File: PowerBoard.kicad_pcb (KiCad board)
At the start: 2 copper layers, 131 x 131 mm, 94 parts, among them IC1 LTC7004HMSE#PBF, IC2 LTC7004HMSE#PBF, IC3 LTC7004HMSE#PBF, J1 XT90, J10 DEAN_T, J11 DEAN_T, J12 DEAN_T, J13 DEAN_T, J14 DEAN_T, J15 DEAN_T, J16 XT60, J17 XT60, J18 XT60, J19 XT60, J2 DEAN_T, J20 XT60, J21 XT60, J22 XT30, J23 XT30, J24 XT30, J25 XT30, J26 XT30, J27 XT30, J28 XT90, J29 XT30, J3 XT60, J30 XT30, J31 XT30, J32 Conn_01x02, J4 XT30, J5 XT90, J6 XT90, J7 XT90, J8 XT90, J9 XT90, Q1 IRFS7437TRLPBF, Q2 IRFS7437TRLPBF, Q3 IRFS7437TRLPBF, U1 Pico, U2 LM317_TO-220

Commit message: iterate the layoutL
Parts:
- added C8: 1u, Capacitor_SMD:C_1206_3216Metric, F.Cu at (86.0, 45.0)
- added D13: LED, Diode_SMD:D_1206_3216Metric, F.Cu at (97.6, 73.5)
- added D14: LED, Diode_SMD:D_1206_3216Metric, F.Cu at (101.4, 84.5)
- added D17: LED, Diode_SMD:D_1206_3216Metric, F.Cu at (52.1, 38.5)
- added F4: Fuse, Fuse:Fuse_Blade_ATO_directSolder, F.Cu at (90.5, 78.5)
- added IC4: LT1910ES8#PBF, SamacSys_Parts:SOIC127P599X175-8N, F.Cu at (92.0, 46.5)
- added Q4: IRFS7437TRLPBF, Package_TO_SOT_SMD:TO-263-2, F.Cu at (92.0, 62.0)
- added R5: 6k8, Resistor_SMD:R_1206_3216Metric, F.Cu at (103.0, 73.5)
- added R6: 6k8, Resistor_SMD:R_1206_3216Metric, F.Cu at (106.5, 84.5)
- added R7: 3m, Resistor_SMD:R_Shunt_Isabellenhuette_BVR4026, F.Cu at (101.2, 49.5)
- added R8: 3m, Resistor_SMD:R_Shunt_Isabellenhuette_BVR4026, F.Cu at (34.7, 37.8)
- C5: value 0.1u -> 1u
- D6: value SMAJ58CA -> SMAJ48A
- D7: value LED -> SMAJ48A; footprint Diode_SMD:D_1206_3216Metric -> Diode_SMD:D_SMA
- IC1: value LTC7004HMSE#PBF -> LT1910ES8#PBF; footprint SamacSys_Parts:SOP50P490X110-11N -> SamacSys_Parts:SOIC127P599X175-8N
- moved R10 91.5 mm to (53.0, 30.8), turned to 0 degrees
- moved D7 87.7 mm to (50.4, 15.8)
- moved D10 87.2 mm to (52.1, 35.1), turned to 0 degrees
- moved R9 74.0 mm to (53.0, 27.5), turned to 0 degrees
- moved F1 69.2 mm to (169.2, 78.5)
- moved D6 49.3 mm to (56.7, 115.4)
- moved Q1 43.7 mm to (39.3, 19.7), turned to 0 degrees
- moved D8 40.3 mm to (57.1, 93.5), turned to 180 degrees
- moved C5 39.4 mm to (49.1, 19.7), turned to 0 degrees
- moved D9 36.2 mm to (67.5, 70.9)
- moved R2 32.8 mm to (72.0, 80.5)
- moved R1 25.4 mm to (64.0, 84.5), turned to 0 degrees
- moved Q2 18.5 mm to (27.8, 89.9)
- moved J2 13.4 mm to (114.5, 45.8), turned to 180 degrees
- moved F2 9.15 mm to (113.8, 78.5), turned to 0 degrees
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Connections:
- C5 pad 1: Net-(IC1-BST) -> Net-(IC1-GND)
- C5 pad 2: Net-(IC1-TS) -> GND
- D10 pad 2: 24V_2 -> Net-(D10-A)
- D6 pad 1: GND -> Net-(D6-A1)
- D6 pad 2: 42V_2 -> GND
- D7 pad 1: Net-(D7-K) -> Net-(D7-A1)
- D7 pad 2: Net-(D7-A) -> GND
- F2 pad 1: Net-(D7-A) -> Net-(D10-A)
- IC1 pad 1: +12V -> Net-(IC1-GND)
- IC1 pad 2: GND -> Net-(IC1-GND)
- IC1 pad 3: GND -> unconnected-(IC1-~{FAULT}-Pad3)
- IC1 pad 5: GND -> Net-(D7-A1)
- IC1 pad 6: Net-(IC1-TGDN) -> Net-(IC1-SENSE)
- IC1 pad 7: Net-(IC1-TGDN) -> unconnected-(IC1-NC-Pad7)
- IC1 pad 8: Net-(IC1-TS) -> Net-(D7-A1)
- Q1 pad 1: Net-(IC1-TGDN) -> Net-(D7-A1)
- Q1 pad 2: Net-(D7-A) -> Net-(D10-A)
- Q1 pad 3: +24V -> Net-(Q1-S)
- R10 pad 1: Net-(D10-K) -> Net-(D17-K)
- R9 pad 1: Net-(D7-K) -> Net-(D10-K)
- U1 pad 9: EN_48V -> EN_42V
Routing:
- net 5V_2: track 279.0 -> 101.4 mm, vias 4 -> 2
- net 42V_2: track 0.00 -> 174.0 mm, vias 0 -> 2
- net EN_42V: track 0.00 -> 129.6 mm, vias 0 -> 1
- net EN_48V: track 123.5 -> 0.00 mm
- net GND: track 954.6 -> 887.1 mm, vias 1 -> 21
- net Net-(D6-A1): track 0.00 -> 24.0 mm
- net Net-(D13-A): track 0.00 -> 22.2 mm
- net Net-(D7-A): track 16.4 -> 0.00 mm
- net Net-(D8-A): track 16.1 -> 0.00 mm
- net Net-(D11-A): track 14.0 -> 0.00 mm
- net +42V: track 84.0 -> 72.6 mm
- net Net-(IC4-SENSE): track 0.00 -> 8.35 mm
- net Net-(Q4-S): track 0.00 -> 6.88 mm
- net 24V_2: track 167.5 -> 162.2 mm
- net Net-(IC4-GND): track 0.00 -> 4.82 mm
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
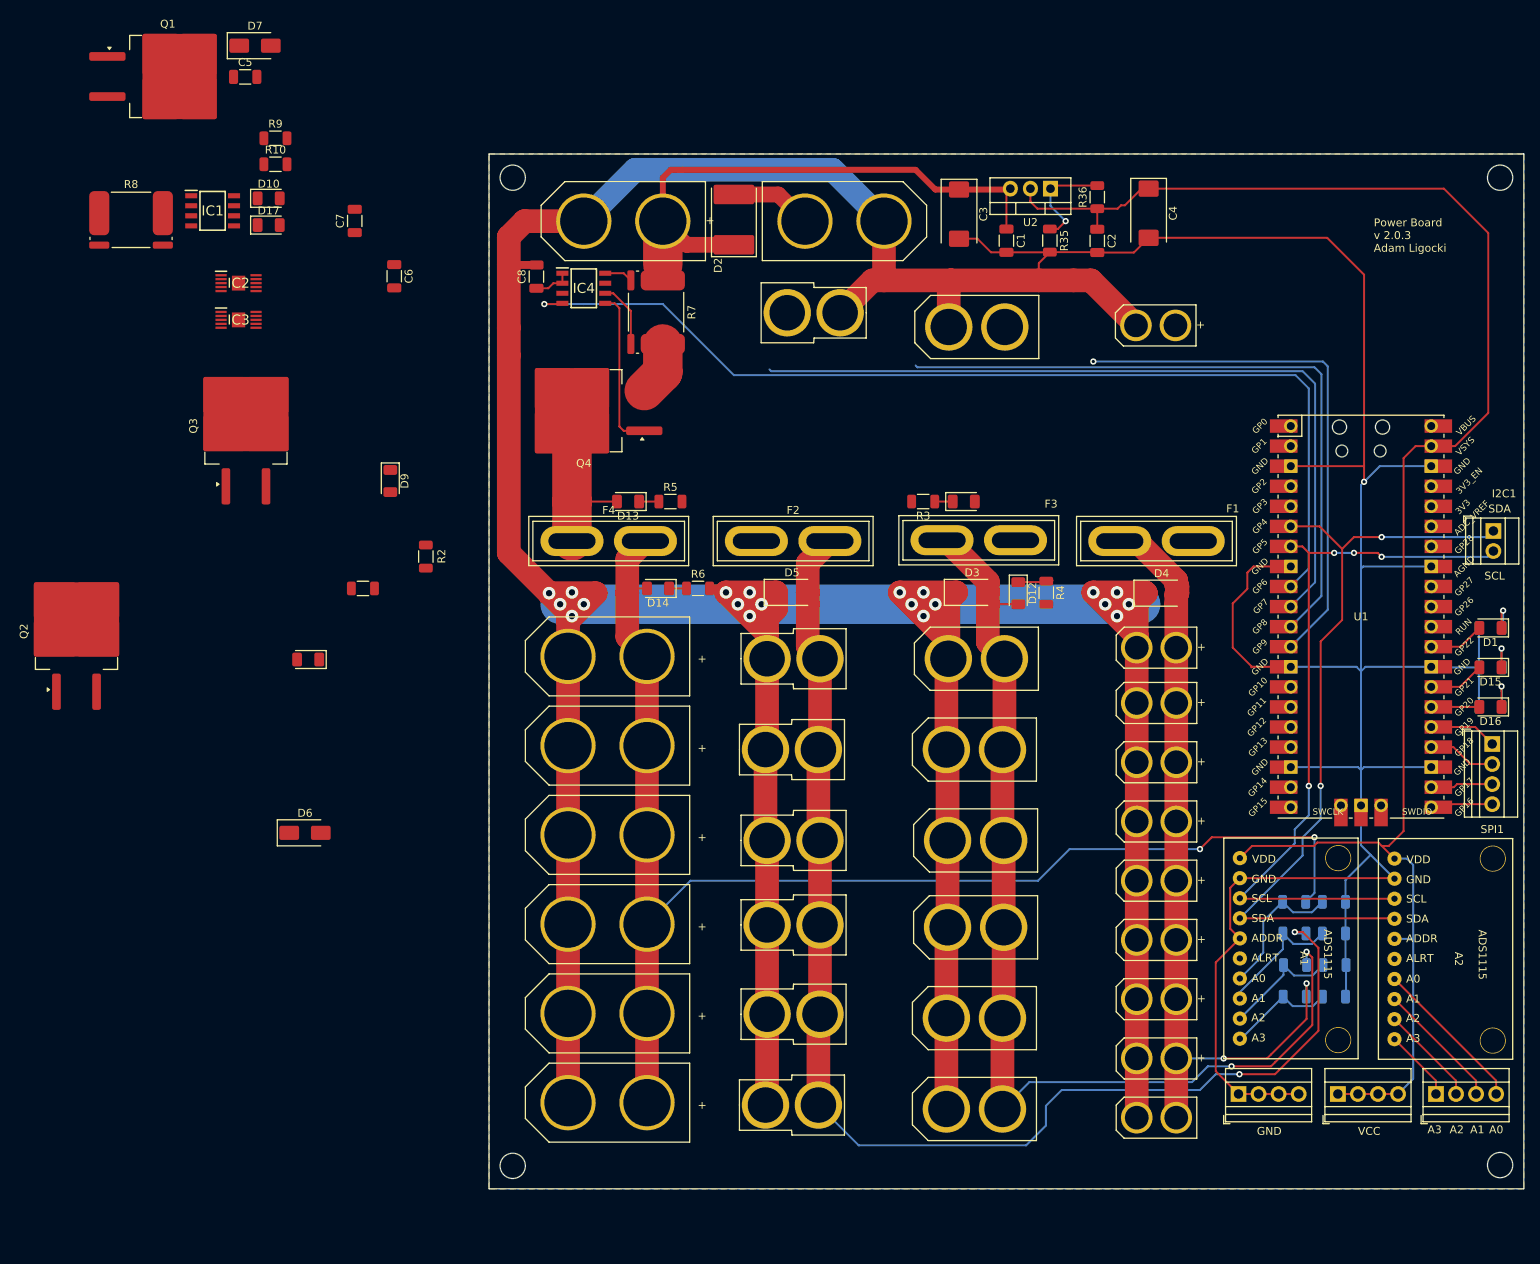
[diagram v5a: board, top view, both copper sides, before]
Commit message: fix the layout
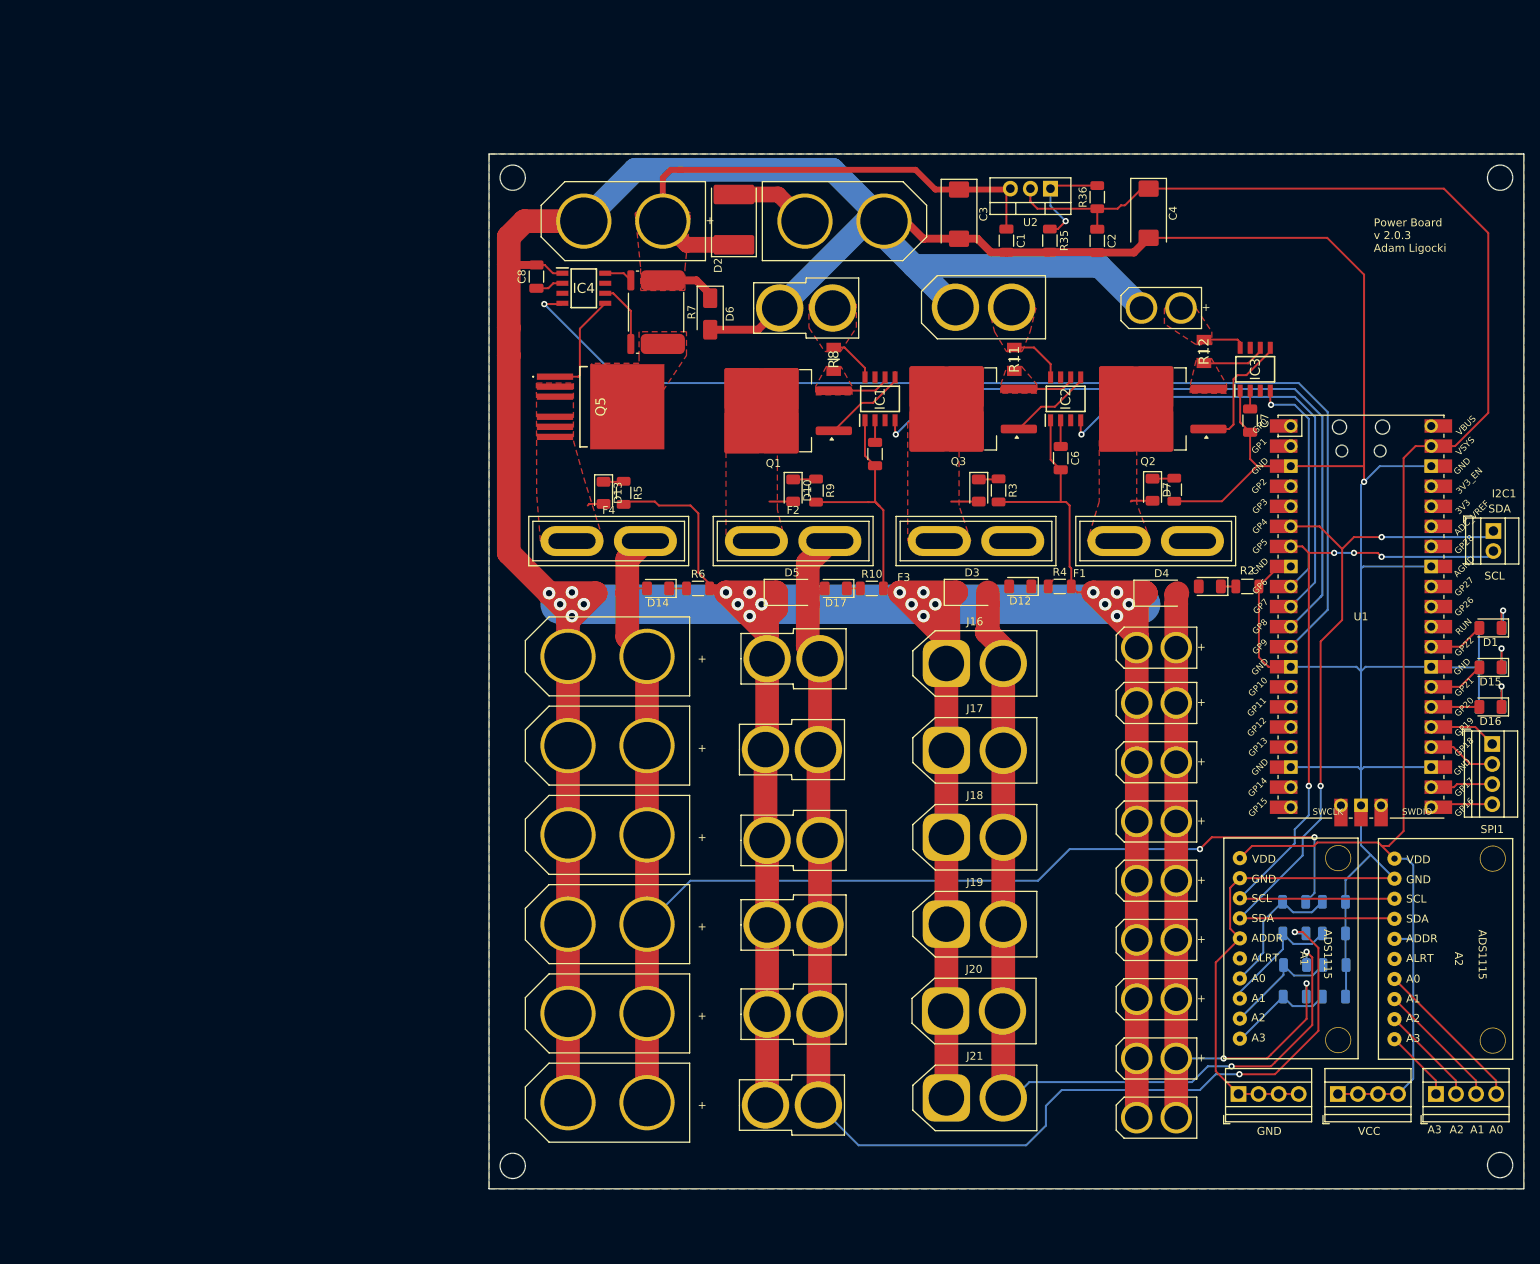
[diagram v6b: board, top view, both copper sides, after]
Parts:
- removed D9: LED, Diode_SMD:D_1206_3216Metric
- removed Q4: IRFS7437TRLPBF, Package_TO_SOT_SMD:TO-263-2
- added Q5: IRFS7530-7PPBF, SamacSys_Parts:IRFS41157PPBF, F.Cu at (94.1, 61.5)
- added R11: 5m, SamacSys_Parts:RESC3216X89N, F.Cu at (146.5, 55.5)
- added R12: 5m, SamacSys_Parts:RESC3216X89N, F.Cu at (170.5, 54.5)
- C6, C7: value 0.1u -> 1u
- D7: value SMAJ48A -> LED; footprint Diode_SMD:D_SMA -> Diode_SMD:D_1206_3216Metric
- IC2, IC3: value LTC7004HMSE#PBF -> LT1910ES8#PBF; footprint SamacSys_Parts:SOP50P490X110-11N -> SamacSys_Parts:SOIC127P599X175-8N
- J16, J17, J18, J19, J20, J21: footprint my_footprint_lib:XT60 -> Connector_AMASS:AMASS_XT60-F_1x02_P7.20mm_Vertical
- R7: value 3m -> 4m
- R8: value 3m -> 1m; footprint Resistor_SMD:R_Shunt_Isabellenhuette_BVR4026 -> SamacSys_Parts:RESC3216X89N
- moved Q2 138.5 mm to (163.4, 61.8), turned to 180 degrees
- moved IC3 128.9 mm to (177.0, 56.8), turned to 90 degrees
- moved D7 126.8 mm to (164.0, 72.0), turned to -90 degrees
- moved C7 116.1 mm to (176.3, 63.3), turned to -90 degrees
- moved D8 114.5 mm to (171.2, 84.2)
- moved IC2 105.7 mm to (153.0, 60.5), turned to 90 degrees
- moved R2 104.1 mm to (176.0, 84.2), turned to 0 degrees
- moved R1 103.5 mm to (166.8, 72.0), turned to -90 degrees
- moved C5 92.9 mm to (128.9, 67.5), turned to -90 degrees
- moved R10 92.7 mm to (128.5, 84.5)
- moved R8 90.7 mm to (123.6, 55.5), turned to 90 degrees
- moved Q3 90.2 mm to (139.4, 61.8), turned to 180 degrees
- moved IC1 87.8 mm to (129.5, 60.5), turned to 90 degrees
- moved Q1 87.6 mm to (116.0, 62.0), turned to 180 degrees
- moved C6 87.5 mm to (152.4, 68.0)
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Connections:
- C5 pad 1: Net-(IC1-GND) -> Net-(IC1-TIMER)
- C6 pad 1: Net-(IC2-BST) -> Net-(IC2-TIMER)
- C6 pad 2: Net-(IC2-TS) -> GND
- C7 pad 1: Net-(IC3-BST) -> Net-(IC3-TIMER)
- C7 pad 2: Net-(IC3-TS) -> GND
- C8 pad 1: Net-(IC4-GND) -> Net-(IC4-TIMER)
- D6 pad 1: Net-(D6-A1) -> +42V
- D7 pad 1: Net-(D7-A1) -> Net-(D7-K)
- D7 pad 2: GND -> Net-(D7-A)
- D8 pad 2: Net-(D8-A) -> 5V_2
- F1 pad 1: Net-(D8-A) -> Net-(D7-A)
- IC1 pad 1: Net-(IC1-GND) -> GND
- IC1 pad 2: Net-(IC1-GND) -> Net-(IC1-TIMER)
- IC1 pad 5: Net-(D7-A1) -> Net-(IC1-GATE)
- IC1 pad 8: Net-(D7-A1) -> +24V
- IC2 pad 1: +12V -> GND
- IC2 pad 2: GND -> Net-(IC2-TIMER)
- IC2 pad 3: GND -> unconnected-(IC2-~{FAULT}-Pad3)
- IC2 pad 4: EN_5V -> EN_12V
- IC2 pad 5: GND -> Net-(IC2-GATE)
- IC2 pad 6: Net-(IC2-TGDN) -> Net-(IC2-SENSE)
- IC2 pad 7: Net-(IC2-TGDN) -> unconnected-(IC2-NC-Pad7)
- IC2 pad 8: Net-(IC2-TS) -> +12V
- IC3 pad 1: +12V -> GND
- IC3 pad 2: GND -> Net-(IC3-TIMER)
- IC3 pad 3: GND -> unconnected-(IC3-~{FAULT}-Pad3)
- IC3 pad 4: EN_12V -> EN_5V
- IC3 pad 5: GND -> Net-(IC3-GATE)
- IC3 pad 6: Net-(IC3-TGDN) -> Net-(IC3-SENSE)
- IC3 pad 7: Net-(IC3-TGDN) -> unconnected-(IC3-NC-Pad7)
- IC3 pad 8: Net-(IC3-TS) -> +5V
- IC4 pad 1: Net-(IC4-GND) -> GND
- IC4 pad 2: Net-(IC4-GND) -> Net-(IC4-TIMER)
- IC4 pad 5: Net-(D6-A1) -> Net-(IC4-GATE)
- IC4 pad 8: Net-(D6-A1) -> Net-(IC4-V+)
- J16 pad 1: 12V_2 -> GND
- J16 pad 2: GND -> 12V_2
- J17 pad 1: 12V_2 -> GND
- J17 pad 2: GND -> 12V_2
- J18 pad 1: 12V_2 -> GND
- J18 pad 2: GND -> 12V_2
- J19 pad 1: 12V_2 -> GND
- J19 pad 2: GND -> 12V_2
- J20 pad 1: 12V_2 -> GND
- J20 pad 2: GND -> 12V_2
- J21 pad 1: 12V_2 -> GND
- J21 pad 2: GND -> 12V_2
- Q1 pad 1: Net-(D7-A1) -> Net-(IC1-GATE)
- Q1 pad 3: Net-(Q1-S) -> Net-(IC1-SENSE)
- Q2 pad 1: Net-(IC2-TGDN) -> Net-(IC3-GATE)
- Q2 pad 2: Net-(D8-A) -> Net-(D7-A)
- Q2 pad 3: +5V -> Net-(IC3-SENSE)
- Q3 pad 1: Net-(IC3-TGDN) -> Net-(IC2-GATE)
- Q3 pad 3: +12V -> Net-(IC2-SENSE)
- R1 pad 1: Net-(D8-K) -> Net-(D7-K)
- R2 pad 1: Net-(D9-K) -> Net-(D8-K)
- R7 pad 1: Net-(Q4-S) -> +42V
- R7 pad 2: Net-(IC4-SENSE) -> Net-(IC4-V+)
- R7 pad 3: Net-(D6-A1) -> Net-(IC4-SENSE)
- R7 pad 4: +42V -> Net-(Q5-D)
- R8 pad 1: Net-(Q1-S) -> Net-(IC1-SENSE)
- R8 pad 2: Net-(IC1-SENSE) -> +24V
- U1 pad 10: EN_24V -> EN_12V
- U1 pad 11: EN_12V -> EN_24V
- U1 pad 12: EN_5V -> EN_42V
- U1 pad 9: EN_42V -> EN_5V
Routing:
- net GND: track 887.1 -> 1017.3 mm
- net EN_5V: track 67.4 -> 29.5 mm
- net EN_12V: track 85.4 -> 59.7 mm, vias 0 -> 1
- net Net-(D6-A1): track 24.0 -> 0.00 mm
- net Net-(D13-A): track 22.2 -> 2.08 mm
- net Net-(IC3-GATE): track 0.00 -> 15.7 mm
- net 12V_2: track 134.6 -> 119.8 mm
- net Net-(IC4-GATE): track 0.00 -> 13.7 mm
- net Net-(IC1-GATE): track 0.00 -> 11.5 mm
- net EN_24V: track 99.3 -> 88.0 mm, vias 0 -> 1
- net Net-(IC2-GATE): track 0.00 -> 10.8 mm
- net 5V_2: track 101.4 -> 91.5 mm
- net EN_42V: track 129.6 -> 138.8 mm
- net Net-(IC3-SENSE): track 0.00 -> 8.20 mm
- net Net-(IC1-SENSE): track 0.00 -> 7.43 mm
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- added copper zone on F.Cu, net +12V
- added copper zone on F.Cu, net +24V
- added copper zone on F.Cu, net +42V
- added copper zone on F.Cu, net +5V
- added copper zone on F.Cu, net Net-(D10-A)
- added copper zone on F.Cu, net Net-(D11-A)
- added copper zone on F.Cu, net Net-(D13-A)
- added copper zone on F.Cu, net Net-(D7-A)
- added copper zone on F.Cu, net Net-(IC1-SENSE)
- added copper zone on F.Cu, net Net-(IC2-SENSE)
- added copper zone on F.Cu, net Net-(IC3-SENSE)
- added copper zone on F.Cu, net Net-(Q5-D)

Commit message: Finish the design
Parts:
- removed A1, A2: ADS1115_ADC_Module, my_footprint_lib:ADS1115
- removed ADC1, SPI1: Screw_Terminal_01x04, TerminalBlock:TerminalBlock_Xinya_XY308-2.54-4P_1x04_P2.54mm_Horizontal
- removed C6: 1u, Capacitor_SMD:C_1206_3216Metric
- removed R25, R32: 100k, Resistor_SMD:R_1206_3216Metric
- removed R30: 33k, Resistor_SMD:R_1206_3216Metric
- removed R31, R33, R39, R40: 10k, Resistor_SMD:R_1206_3216Metric
- removed R35: 680R, Resistor_SMD:R_1206_3216Metric
- removed R36: 220R, Resistor_SMD:R_1206_3216Metric
- added C10: 22pF, Capacitor_SMD:C_1206_3216Metric, F.Cu at (147.0, 33.5)
- added C11: 3300pF, Capacitor_SMD:C_1206_3216Metric, F.Cu at (149.5, 33.5)
- added C12: 10u, Capacitor_SMD:C_1206_3216Metric, F.Cu at (141.0, 24.5)
- added C13: 1u, Capacitor_SMD:C_1206_3216Metric, F.Cu at (130.0, 26.0)
- added C9: 5.5nF, Capacitor_SMD:C_1206_3216Metric, F.Cu at (144.5, 33.5)
- added D18: LED, Diode_SMD:D_1206_3216Metric, F.Cu at (168.5, 76.5)
- added D19: LED, Diode_SMD:D_1206_3216Metric, F.Cu at (168.5, 82.0)
- added D9: SMAJ30CA, Diode_SMD:D_SMA, F.Cu at (68.0, 74.0)
- added F5: Fuse, Fuse:Fuse_Blade_ATO_directSolder, F.Cu at (54.4, 67.0)
- added G***: LOGO, LOGO, F.Cu at (152.5, 153.5)
- added H5: MountingHole, MountingHole:MountingHole_3.2mm_M3, F.Cu at (100.2, 93.0)
- added IC5: LT1910ES8#PBF, SamacSys_Parts:SOIC127P599X175-8N, F.Cu at (67.5, 60.0)
- added IC7: MAX17541GATB+T, SamacSys_Parts:SON50P200X300X80-11N, F.Cu at (141.6, 29.1)
- added J33: XT30, Connector_AMASS:AMASS_XT30U-F_1x02_P5.0mm_Vertical, F.Cu at (117.5, 88.5)
- added J34: XT30, Connector_AMASS:AMASS_XT30U-F_1x02_P5.0mm_Vertical, F.Cu at (117.5, 95.5)
- added J35: XT30, Connector_AMASS:AMASS_XT30U-F_1x02_P5.0mm_Vertical, F.Cu at (117.5, 102.5)
- added J36: XT30, Connector_AMASS:AMASS_XT30U-F_1x02_P5.0mm_Vertical, F.Cu at (117.5, 109.5)
- added J37: XT30, Connector_AMASS:AMASS_XT30U-F_1x02_P5.0mm_Vertical, F.Cu at (117.5, 116.5)
- added J38: XT30, Connector_AMASS:AMASS_XT30U-F_1x02_P5.0mm_Vertical, F.Cu at (117.5, 123.5)
- added J39: XT30, Connector_AMASS:AMASS_XT30U-F_1x02_P5.0mm_Vertical, F.Cu at (117.5, 130.5)
- added J40: XT30, Connector_AMASS:AMASS_XT30U-F_1x02_P5.0mm_Vertical, F.Cu at (117.5, 137.5)
- added J41: XT60, Connector_AMASS:AMASS_XT60-F_1x02_P7.20mm_Vertical, F.Cu at (76.5, 37.5)
- added L1: 470M, SamacSys_Parts:SRR5828A2R6Y, F.Cu at (147.5, 23.6)
- added Q4: IRFS7437TRLPBF, Package_TO_SOT_SMD:TO-263-2, F.Cu at (97.5, 51.0)
- added R13: 6k8, Resistor_SMD:R_1206_3216Metric, F.Cu at (98.5, 73.5)
- added R14: 5m, SamacSys_Parts:RESC3216X89N, F.Cu at (104.0, 44.5)
- added R15: 6k8, Resistor_SMD:R_1206_3216Metric, F.Cu at (57.0, 73.0)
- added R16: 80k, Resistor_SMD:R_1206_3216Metric, F.Cu at (140.0, 33.5)
- added R17: 17.5k, Resistor_SMD:R_1206_3216Metric, F.Cu at (135.5, 33.0)
- added R18: 10k, Resistor_SMD:R_1206_3216Metric, F.Cu at (170.0, 47.0)
- added R19: 10k, Resistor_SMD:R_1206_3216Metric, F.Cu at (167.0, 47.0)
- added R20: 10k, Resistor_SMD:R_1206_3216Metric, B.Cu at (141.5, 99.0)
- added R21: 21.5k, Resistor_SMD:R_1206_3216Metric, F.Cu at (148.0, 30.0)
- added R22: 10k, Resistor_SMD:R_1206_3216Metric, F.Cu at (171.5, 71.0)
- added R23: 10k, Resistor_SMD:R_1206_3216Metric, F.Cu at (171.5, 76.5)
- added R24: 10k, Resistor_SMD:R_1206_3216Metric, F.Cu at (171.5, 82.0)
- added U3: INA238, Package_SO:VSSOP-10_3x3mm_P0.5mm, F.Cu at (96.0, 27.0)
- added U4: INA238, Package_SO:VSSOP-10_3x3mm_P0.5mm, F.Cu at (105.0, 27.0)
- added U5: INA238, Package_SO:VSSOP-10_3x3mm_P0.5mm, F.Cu at (114.0, 27.0)
- added U6: INA238, Package_SO:VSSOP-10_3x3mm_P0.5mm, F.Cu at (123.0, 27.0)
- C3, C4: value 10u -> 1u; footprint Capacitor_Tantalum_SMD:CP_EIA-7343-15_Kemet-W -> Capacitor_SMD:C_1206_3216Metric
- D1: value LED -> SMAJ48A; footprint Diode_SMD:D_1206_3216Metric -> Diode_SMD:D_SMA
- D10: value LED -> SMAJ30CA; footprint Diode_SMD:D_1206_3216Metric -> Diode_SMD:D_SMA
- D11: value LED -> SMAJ15CA; footprint Diode_SMD:D_1206_3216Metric -> Diode_SMD:D_SMA
- D14: value LED -> SMAJ6.5CA; footprint Diode_SMD:D_1206_3216Metric -> Diode_SMD:D_SMA
- D3: value SMAJ15CA -> LED; footprint Diode_SMD:D_SMA -> Diode_SMD:D_1206_3216Metric
- D4: value SMAJ6.5CA -> LED; footprint Diode_SMD:D_SMA -> Diode_SMD:D_1206_3216Metric
- D5: value SMAJ30CA -> LED; footprint Diode_SMD:D_SMA -> Diode_SMD:D_1206_3216Metric
- D6: value SMAJ48A -> LED; footprint Diode_SMD:D_SMA -> Diode_SMD:D_1206_3216Metric
- J1, J6, J7, J8, J9: footprint my_footprint_lib:XT90 -> SamacSys_Parts:XT90
- J10, J11, J12, J13: value DEAN_T -> XT90; footprint my_footprint_lib:DEAN_T -> SamacSys_Parts:XT90
- J14, J15, J2: footprint my_footprint_lib:DEAN_T -> SamacSys_Parts:DEANS-T
- J16, J17, J18, J19: value XT60 -> DEAN_T; footprint Connector_AMASS:AMASS_XT60-F_1x02_P7.20mm_Vertical -> SamacSys_Parts:DEANS-T
- J22, J23, J24, J25, J26, J27, J29, J30, J31: value XT30 -> XT60; footprint my_footprint_lib:XT30 -> Connector_AMASS:AMASS_XT60-F_1x02_P7.20mm_Vertical
- J28: value XT90 -> XT60; footprint my_footprint_lib:XT90 -> Connector_AMASS:AMASS_XT60-F_1x02_P7.20mm_Vertical
- J3: footprint my_footprint_lib:XT60 -> Connector_AMASS:AMASS_XT60-F_1x02_P7.20mm_Vertical
- J32: value Conn_01x02 -> XT30; footprint my_footprint_lib:XT90 -> Connector_AMASS:AMASS_XT30U-F_1x02_P5.0mm_Vertical
- J5: value XT90 -> Conn_01x02; footprint my_footprint_lib:XT90 -> SamacSys_Parts:XT90
- Q1: value IRFS7437TRLPBF -> IRFS7530TRL7PP; footprint Package_TO_SOT_SMD:TO-263-2 -> SamacSys_Parts:IRFS7530TRL7PP
- Q5: value IRFS7530-7PPBF -> IRFS7437TRLPBF; footprint SamacSys_Parts:IRFS41157PPBF -> Package_TO_SOT_SMD:TO-263-2
- R1: value 6k8 -> 4m; footprint Resistor_SMD:R_1206_3216Metric -> Resistor_SMD:R_Shunt_Isabellenhuette_BVR4026
- R11: value 5m -> 1m
- R12: value 5m -> 6k8; footprint SamacSys_Parts:RESC3216X89N -> Resistor_SMD:R_1206_3216Metric
- R27, R29: value 100k -> 10k
- R7: value 4m -> 5m; footprint Resistor_SMD:R_Shunt_Isabellenhuette_BVR4026 -> SamacSys_Parts:RESC3216X89N
- R8: value 1m -> 5m
- U2: value LM317_TO-220 -> INA238; footprint Package_TO_SOT_THT:TO-220-3_Vertical -> Package_SO:VSSOP-10_3x3mm_P0.5mm
- moved D1 162.0 mm to (53.0, 38.5), turned to -90 degrees
- moved D16 149.6 mm to (59.5, 73.0), turned to 90 degrees
- moved IC3 141.7 mm to (37.0, 35.0), turned to 0 degrees
- moved D8 132.2 mm to (39.5, 73.0), turned to 90 degrees
- moved R1 124.5 mm to (47.0, 38.0)
- moved R4 114.8 mm to (40.0, 60.0), turned to -90 degrees
- moved R12 110.6 mm to (60.0, 60.0)
- moved C3 108.5 mm to (31.0, 34.0), turned to 90 degrees
- moved D15 107.8 mm to (101.0, 73.5), turned to 90 degrees
- moved F3 103.8 mm to (33.9, 67.0)
- moved R2 97.6 mm to (81.5, 60.0), turned to -90 degrees
- moved J15 91.4 mm to (58.0, 91.5)
- moved J14 90.9 mm to (58.0, 81.0)
- moved J25 87.2 mm to (73.9, 133.5)
- moved J24 86.6 mm to (73.9, 123.0)
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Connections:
- C1 pad 1: +42V -> Net-(IC1-TIMER)
- C2 pad 1: VCC -> Net-(IC2-TIMER)
- C3 pad 1: +42V -> Net-(IC3-TIMER)
- C4 pad 1: VCC -> Net-(IC4-TIMER)
- C5 pad 1: Net-(IC1-TIMER) -> Net-(IC5-TIMER)
- C7 pad 1: Net-(IC3-TIMER) -> +42V
- C8 pad 1: Net-(IC4-TIMER) -> Net-(IC7-VCC)
- D1 pad 1: Net-(D1-K) -> +42V
- D1 pad 2: Net-(D1-A) -> GND
- D10 pad 1: Net-(D10-K) -> GND
- D10 pad 2: Net-(D10-A) -> 15V_2
- D11 pad 1: Net-(D11-K) -> GND
- D11 pad 2: Net-(D11-A) -> 12V_2
- D12 pad 2: 12V_2 -> Net-(D12-A)
- D14 pad 1: Net-(D14-K) -> 5V_2
- D14 pad 2: 42V_2 -> GND
- D15 pad 2: Net-(D15-A) -> 12V_2
- D16 pad 2: Net-(D16-A) -> 24V_2
- D17 pad 2: 24V_2 -> Net-(D17-A)
- D3 pad 1: GND -> Net-(D3-K)
- D3 pad 2: 12V_2 -> Net-(D3-A)
- D4 pad 1: GND -> Net-(D4-K)
- D4 pad 2: 5V_2 -> Net-(D4-A)
- D5 pad 1: GND -> Net-(D5-K)
- D5 pad 2: 24V_2 -> Net-(D5-A)
- D6 pad 1: +42V -> Net-(D6-K)
- D6 pad 2: GND -> 15V_2
- D7 pad 2: Net-(D7-A) -> 5V_2
- D8 pad 2: 5V_2 -> 42V_2
- F1 pad 1: Net-(D7-A) -> Net-(D3-A)
- F1 pad 2: 5V_2 -> 15V_2
- F2 pad 1: Net-(D10-A) -> Net-(D4-A)
- F2 pad 2: 24V_2 -> 5V_2
- F3 pad 1: Net-(D11-A) -> Net-(D5-A)
- F3 pad 2: 12V_2 -> 42V_2
- F4 pad 1: Net-(D13-A) -> Net-(D12-A)
- F4 pad 2: 42V_2 -> 12V_2
- IC1 pad 3: unconnected-(IC1-~{FAULT}-Pad3) -> FAULT_15V
- IC1 pad 4: EN_24V -> EN_15V
- IC1 pad 6: Net-(IC1-SENSE) -> CURR_3-
- IC1 pad 8: +24V -> CURR_3+
- IC2 pad 3: unconnected-(IC2-~{FAULT}-Pad3) -> FAULT_5V
- IC2 pad 4: EN_12V -> EN_5V
- IC2 pad 6: Net-(IC2-SENSE) -> CURR_5-
- IC2 pad 8: +12V -> CURR_5+
- IC3 pad 3: unconnected-(IC3-~{FAULT}-Pad3) -> FAULT_42V
- IC3 pad 4: EN_5V -> EN_42V
- IC3 pad 6: Net-(IC3-SENSE) -> CURR_1-
- IC3 pad 8: +5V -> CURR_1+
- IC4 pad 3: unconnected-(IC4-~{FAULT}-Pad3) -> FAULT_12V
- IC4 pad 4: EN_42V -> EN_12V
- IC4 pad 6: Net-(IC4-SENSE) -> CURR_4-
- IC4 pad 8: Net-(IC4-V+) -> CURR_4+
- J10 pad 1: 24V_2 -> 42V_2
- J11 pad 1: 24V_2 -> 42V_2
- J12 pad 1: 24V_2 -> 42V_2
- J13 pad 1: 24V_2 -> 42V_2
- J14 pad 1: 24V_2 -> GND
- J14 pad 2: GND -> 24V_2
- J15 pad 1: 24V_2 -> GND
- J15 pad 2: GND -> 24V_2
- J16 pad 2: 12V_2 -> 24V_2
- J17 pad 2: 12V_2 -> 24V_2
- J18 pad 2: 12V_2 -> 24V_2
- J19 pad 2: 12V_2 -> 24V_2
- J2 pad 1: +24V -> GND
- J2 pad 2: GND -> CURR_2+
- J20 pad 2: 12V_2 -> 15V_2
- J21 pad 2: 12V_2 -> 15V_2
- J22 pad 1: 5V_2 -> GND
- J22 pad 2: GND -> 15V_2
- J23 pad 1: 5V_2 -> GND
- J23 pad 2: GND -> 15V_2
- J24 pad 1: 5V_2 -> GND
- J24 pad 2: GND -> 15V_2
- J25 pad 1: 5V_2 -> GND
- J25 pad 2: GND -> 15V_2
- J26 pad 1: 5V_2 -> GND
- J26 pad 2: GND -> 12V_2
- J27 pad 1: 5V_2 -> GND
- J27 pad 2: GND -> 12V_2
- J28 pad 1: 42V_2 -> GND
- J28 pad 2: GND -> 12V_2
- J29 pad 1: 5V_2 -> GND
- J29 pad 2: GND -> 12V_2
- J3 pad 1: +12V -> GND
- J3 pad 2: GND -> CURR_4+
- J30 pad 1: 5V_2 -> GND
- J30 pad 2: GND -> 12V_2
- J31 pad 1: 5V_2 -> GND
- J31 pad 2: GND -> 12V_2
- J32 pad 1: Net-(D2-A) -> GND
- J32 pad 2: GND -> 5V_2
- J4 pad 1: +5V -> CURR_5+
- J5 pad 1: 42V_2 -> Net-(D2-A)
- Q1 pad 1: Net-(IC1-GATE) -> Net-(IC3-GATE)
- Q1 pad 2: Net-(D10-A) -> Net-(D5-A)
- Q1 pad 3: Net-(IC1-SENSE) -> Net-(D5-A)
- Q2 pad 1: Net-(IC3-GATE) -> Net-(IC1-GATE)
- Q2 pad 2: Net-(D7-A) -> Net-(D3-A)
- Q2 pad 3: Net-(IC3-SENSE) -> CURR_3-
- Q3 pad 2: Net-(D11-A) -> Net-(D4-A)
- Q3 pad 3: Net-(IC2-SENSE) -> CURR_5-
- Q5 pad 1: Net-(IC4-GATE) -> Net-(IC5-GATE)
- Q5 pad 3: Net-(D13-A) -> CURR_2-
- R1 pad 1: Net-(D7-K) -> +42V
- R1 pad 2: GND -> CURR_1+
- R10 pad 1: Net-(D17-K) -> Net-(D12-K)
- R11 pad 1: +12V -> CURR_2-
- R11 pad 2: Net-(IC2-SENSE) -> CURR_2+
- R12 pad 1: +5V -> Net-(D13-K)
- R12 pad 2: Net-(IC3-SENSE) -> GND
- R2 pad 1: Net-(D8-K) -> Net-(D3-K)
- R26 pad 1: Net-(A1-A0) -> VCC
- R26 pad 2: GND -> ALERT_2
- R27 pad 1: 24V_2 -> VCC
- R27 pad 2: Net-(A1-A1) -> ALERT_3
- R28 pad 1: Net-(A1-A1) -> VCC
- R28 pad 2: GND -> ALERT_4
- R29 pad 1: 12V_2 -> VCC
- R29 pad 2: Net-(A1-A2) -> ALERT_5
- R3 pad 1: Net-(D11-K) -> Net-(D4-K)
- R4 pad 1: Net-(D12-K) -> Net-(D5-K)
- R5 pad 1: Net-(D13-K) -> Net-(D6-K)
- R6 pad 1: Net-(D14-K) -> Net-(D7-K)
- R7 pad 1: +42V -> CURR_3+
- R7 pad 2: Net-(IC4-V+) -> CURR_3-
- R8 pad 1: Net-(IC1-SENSE) -> CURR_5+
- R8 pad 2: +24V -> CURR_5-
- R9 pad 1: Net-(D10-K) -> Net-(D8-K)
- U1 pad 10: EN_12V -> FAULT_12V
- U1 pad 11: EN_24V -> FAULT_5V
- U1 pad 12: EN_42V -> EN_5V
- U1 pad 14: unconnected-(U1-GPIO10-Pad14) -> EN_12V
- U1 pad 15: unconnected-(U1-GPIO11-Pad15) -> EN_15V
- U1 pad 16: unconnected-(U1-GPIO12-Pad16)_1 -> EN_24V
- U1 pad 17: unconnected-(U1-GPIO13-Pad17)_1 -> EN_42V
- U1 pad 19: unconnected-(U1-GPIO14-Pad19) -> ALERT_1
- U1 pad 20: unconnected-(U1-GPIO15-Pad20)_1 -> ALERT_2
- U1 pad 21: Net-(SPI1-Pin_4) -> ALERT_3
- U1 pad 22: Net-(SPI1-Pin_3) -> ALERT_4
- U1 pad 24: Net-(SPI1-Pin_2) -> ALERT_5
- U1 pad 25: Net-(SPI1-Pin_1) -> unconnected-(U1-GPIO19-Pad25)
- U1 pad 26: Net-(D16-A) -> Net-(D19-A)
- U1 pad 27: Net-(D15-A) -> Net-(D18-A)
- U1 pad 29: Net-(D1-A) -> Net-(D17-A)
- U1 pad 4: unconnected-(U1-GPIO2-Pad4) -> FAULT_42V
- U1 pad 5: unconnected-(U1-GPIO3-Pad5) -> FAULT_24V
- U1 pad 9: EN_5V -> FAULT_15V
- U2 pad 1: Net-(U2-ADJ) -> GND
- U2 pad 2: VCC -> GND
- U2 pad 3: +42V -> ALERT_1
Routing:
- net GND: track 1017.3 -> 1201.6 mm, vias 21 -> 31
- net FAULT_42V: track 0.00 -> 146.0 mm, vias 0 -> 2
- net ALERT_4: track 0.00 -> 134.5 mm, vias 0 -> 2
- net ALERT_5: track 0.00 -> 134.1 mm, vias 0 -> 2
- net ALERT_1: track 0.00 -> 128.2 mm
- net ALERT_3: track 0.00 -> 126.6 mm, vias 0 -> 2
- net ALERT_2: track 0.00 -> 116.7 mm, vias 0 -> 2
- net EN_15V: track 0.00 -> 108.9 mm, vias 0 -> 1
- net FAULT_24V: track 0.00 -> 105.6 mm, vias 0 -> 2
- net 24V_2: track 164.5 -> 76.6 mm, vias 2 -> 0
- net 42V_2: track 174.0 -> 91.7 mm, vias 2 -> 0
- net CURR_3+: track 0.00 -> 79.6 mm, vias 0 -> 4
- net CURR_3-: track 0.00 -> 77.3 mm, vias 0 -> 4
- net 15V_2: track 0.00 -> 77.0 mm
- net CURR_2+: track 0.00 -> 68.8 mm, vias 0 -> 4
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- removed copper zone on F.Cu, net +12V
- removed copper zone on F.Cu, net +24V
- removed copper zone on F.Cu, net +42V
- removed copper zone on F.Cu, net +5V
- removed copper zone on F.Cu, net Net-(D10-A)
- removed copper zone on F.Cu, net Net-(D11-A)
- removed copper zone on F.Cu, net Net-(D13-A)
- removed copper zone on F.Cu, net Net-(D7-A)
- removed copper zone on F.Cu, net Net-(IC1-SENSE)
- removed copper zone on F.Cu, net Net-(IC2-SENSE)
- removed copper zone on F.Cu, net Net-(IC3-SENSE)
- removed copper zone on F.Cu, net Net-(Q5-D)
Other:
- board size 131 x 131 mm -> 150 x 150 mm
- board text added: "Power Board v2.2.0"
- board text removed: "A0"
- board text removed: "A1"
- board text removed: "A2"
- board text removed: "A3"
- board text removed: "GND"
- board text removed: "Power Board v 2.0.3 Adam Ligocki"
- board text removed: "SCL"
- board text removed: "SDA"
- board text removed: "VCC"
